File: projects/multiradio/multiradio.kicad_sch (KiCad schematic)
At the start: 21 parts, among them J1 USB_B

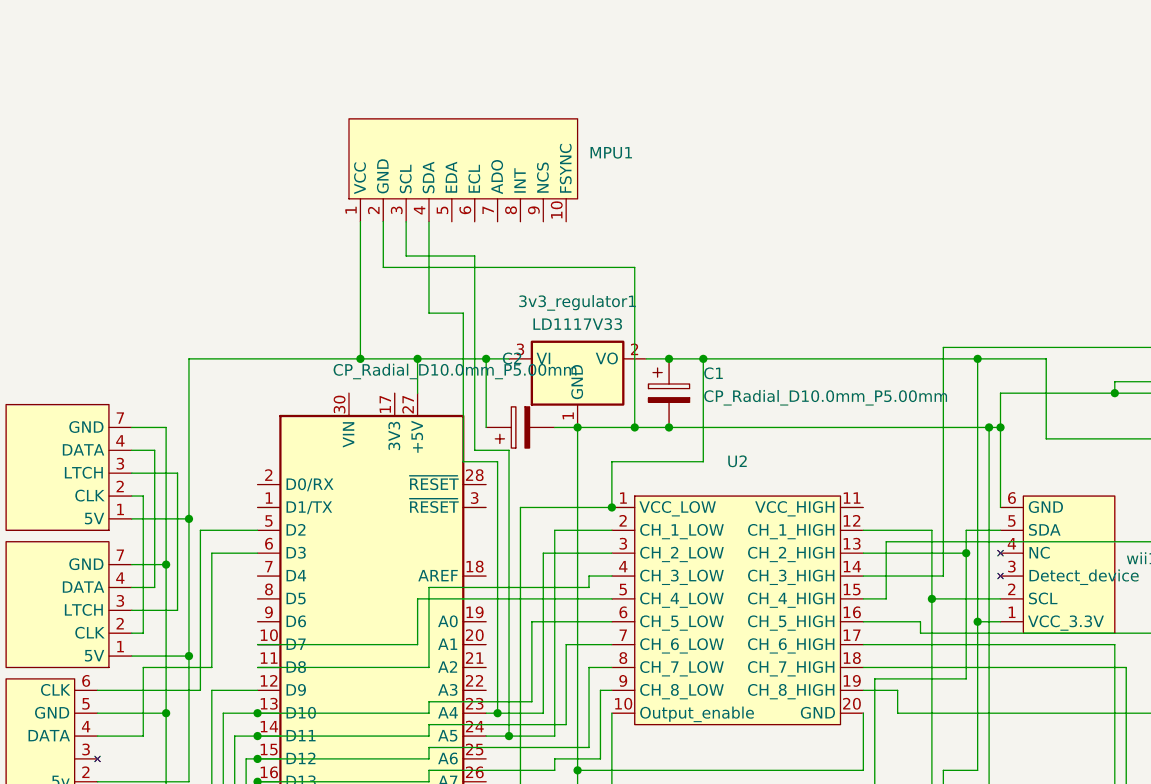
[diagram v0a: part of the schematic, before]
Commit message: update to 3.3v bat radio
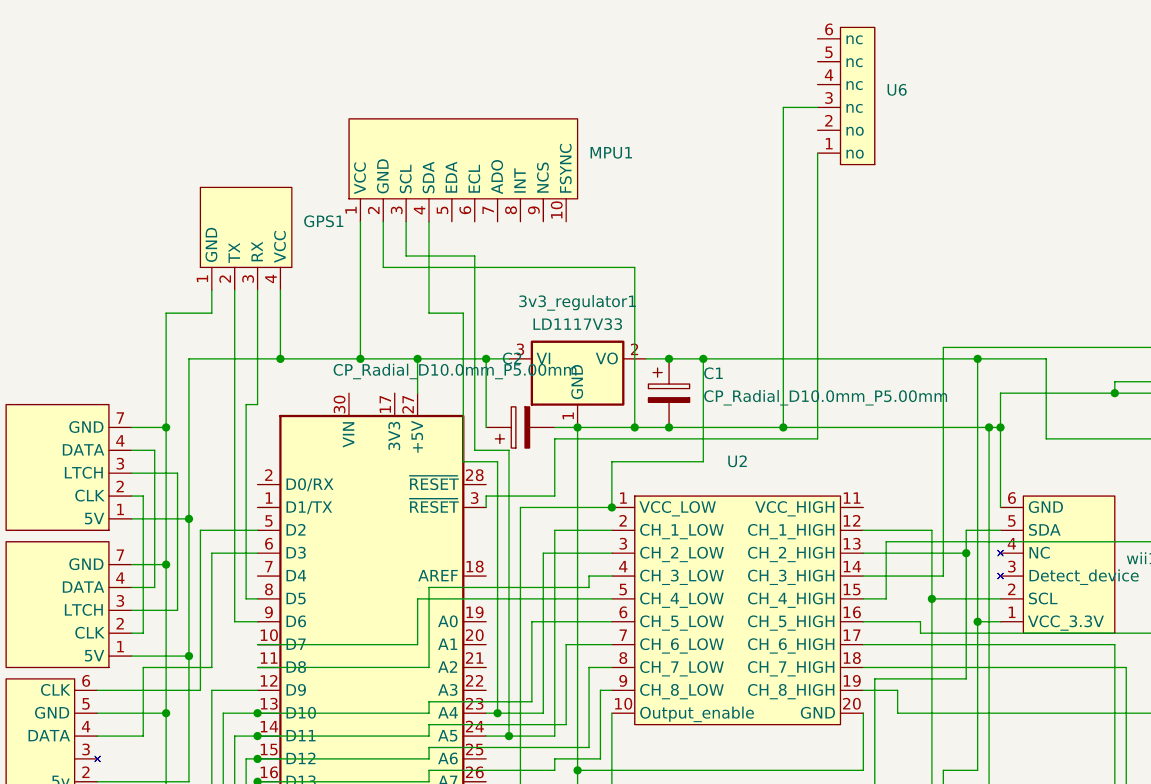
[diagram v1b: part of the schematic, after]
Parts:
- added GPS1: ~, Footprints_cez:GY-NEO6MV2, symbol Symbols_cez:GY-NEO6MV2
- added U6: ~, Footprints_cez:Switch A03 PS-22F03, symbol Symbols_cez:Switch_A03_PS-22F03
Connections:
- net at 3v3_regulator1.1 (GND), A1.29 (GND), A1.4 (GND)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: now also GPS1.1 (GND), U6.3 (nc)
- net at 3v3_regulator1.3 (VI), A1.27 (+5V), C2.1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: now also GPS1.4 (VCC)
- net at A1.3 (~{RESET}): now also U6.1 (no)
- net at A1.8 (D5): now also GPS1.3 (RX)
- net at A1.9 (D6): now also GPS1.2 (TX)

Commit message: only multi remote left
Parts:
- removed GPS1: ~, Footprints_cez:GY-NEO6MV2, symbol Symbols_cez:GY-NEO6MV2
- removed U2: ~, Footprints_cez:TXS0108E, symbol Symbols_cez:TXS0108E_
- removed U6: ~, Footprints_cez:Switch A03 PS-22F03, symbol Symbols_cez:Switch_A03_PS-22F03
- added U2: ~, Footprints_cez:8 Channel Logic Level Converter, symbol Symbols_cez:8_Channel_Logic_Level_Converter
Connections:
- net at Gamecube1.2 (DATA): now also U2.4 (LV4)
- net at 3v3_regulator1.1 (GND), A1.29 (GND), A1.4 (GND)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: now also U2.16 (GND), U2.6 (GND); no longer Playstation1.4 (GND)
- net at 3v3_regulator1.2 (VO), Gamecube1.6 (3.3v), N64_controller1.1 (3.3v)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: now also C2.1, U2.5 (LV); no longer C1.1, Display1.4 (VCC), NRF1.2 (VCC), Playstation1.5 (3.3V)
- net at wii1.2 (SCL): now also U2.2 (LV2); no longer Display1.2 (SCL)
- net at wii1.5 (SDA): now also U2.1 (LV1); no longer Display1.1 (SDA)
- net at 3v3_regulator1.3 (VI), A1.27 (+5V), MPU1.1 (VCC)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: now also C1.1, Display1.4 (VCC), NRF1.2 (VCC), U2.15 (HV); no longer C2.1
- net at A1.24 (A5), MPU1.3 (SCL): now also Display1.2 (SCL), U2.12 (HV2)
- net at A1.23 (A4), MPU1.4 (SDA): now also Display1.1 (SDA), U2.11 (HV1)
- net at A1.10 (D7): now also Nes1.3 (LTCH), Snes1.3 (LTCH)
- net at A1.11 (D8): now also Nes1.2 (CLK), Snes1.2 (CLK)
- net at A1.13 (D10), NRF1.4 (~{CSN}): now also U2.20 (HV8)
- net at A1.14 (D11), NRF1.6 (MOSI): now also U2.17 (HV5)
- net at A1.15 (D12), NRF1.7 (MISO): now also U2.18 (HV6)
- net at A1.16 (D13), NRF1.5 (SCK): now also U2.19 (HV7)
- net at A1.7 (D4): now also U2.14 (HV4)
- net at A1.8 (D5): now also U2.13 (HV3)
- net at A1.9 (D6): now also Nes1.4 (DATA), Snes1.4 (DATA)
- net at N64_controller1.2 (DATA): now also U2.3 (LV3)
- net at Playstation1.6 (ATTN): now also U2.10 (LV8)
- net at Playstation1.2 (CMD): now also U2.7 (LV5)
- net at Playstation1.1 (DATA): now also U2.8 (LV6)
- net at Playstation1.7 (CLK): now also U2.9 (LV7)
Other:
- moved on the sheet: 3v3_regulator1, C1, C2, Display1, Gamecube1, J1, MPU1, N64_controller1, NRF1, Nes1, Playstation1, Snes1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

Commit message: ps2 180 degree
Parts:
- Playstation1: footprint Footprints_cez:Playstation 2 controller 90 degree -> Footprints_cez:Playstation 2 controller 180
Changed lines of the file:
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@@
 			)
 		)
-		(property "Footprint" "Footprints_cez:Playstation 2 controller 90 degree"
+		(property "Footprint" "Footprints_cez:Playstation 2 controller 180"
 			(at 194.564 25.654 0)
 			(effects

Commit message: multiremote done
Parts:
- removed J1: USB_B, Connector_PinHeader_2.54mm:PinHeader_1x04_P2.54mm_Vertical, symbol Connector:USB_B
- removed TP1: TestPoint, Connector_PinHeader_2.54mm:PinHeader_1x01_P2.54mm_Vertical, symbol Connector:TestPoint
- removed U1: ~, Footprints_cez:MH-CD42, symbol Symbols_cez:MH-CD42
- removed U3: ~, Footprints_cez:USB-B, symbol Symbols_cez:usb-b
- removed U4: ~, Footprints_cez:BH-18650-PC2, symbol Symbols_cez:battery
- removed U5: ~, Footprints_cez:Switch A03 PS-22F03, symbol Symbols_cez:Switch_A03_PS-22F03
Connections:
- net at 3v3_regulator1.1 (GND), A1.29 (GND), A1.4 (GND)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: now also Playstation1.4 (GND)
- net at 3v3_regulator1.2 (VO), C2.1, Gamecube1.6 (3.3v)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: now also NRF1.2 (VCC), Playstation1.5 (3.3V)
- net at 3v3_regulator1.3 (VI), A1.27 (+5V), C1.1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: no longer NRF1.2 (VCC)
